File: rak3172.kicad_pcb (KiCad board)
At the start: 4 copper layers, 40 x 30 mm, 82 parts, among them Q1 AO3401, Q2 SI2302, SW1 SW_Push, SW2 SW_Push, U1 AP6683, U2 RAK3172-SiP, U3 TP733xx, U4 UHE4913, U5 QMC6308, U6 L80RE-M37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

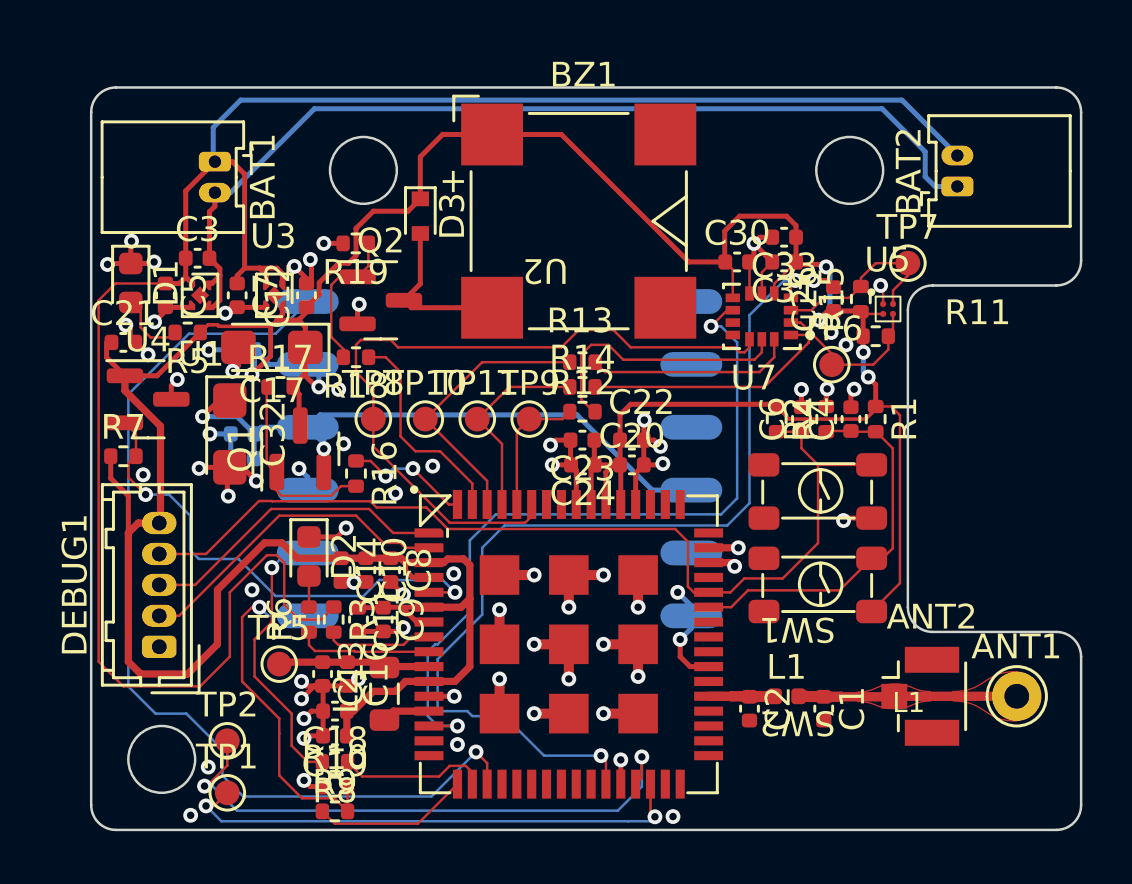
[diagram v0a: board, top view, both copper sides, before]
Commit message: Added 3D Models (-Antenna) Added Manufacturing File (BOM/POS/Gerber) Tidied up silkscreen placement Added via stitching Added via fencing for GCPW Changed bat connector position and package (to SMD)
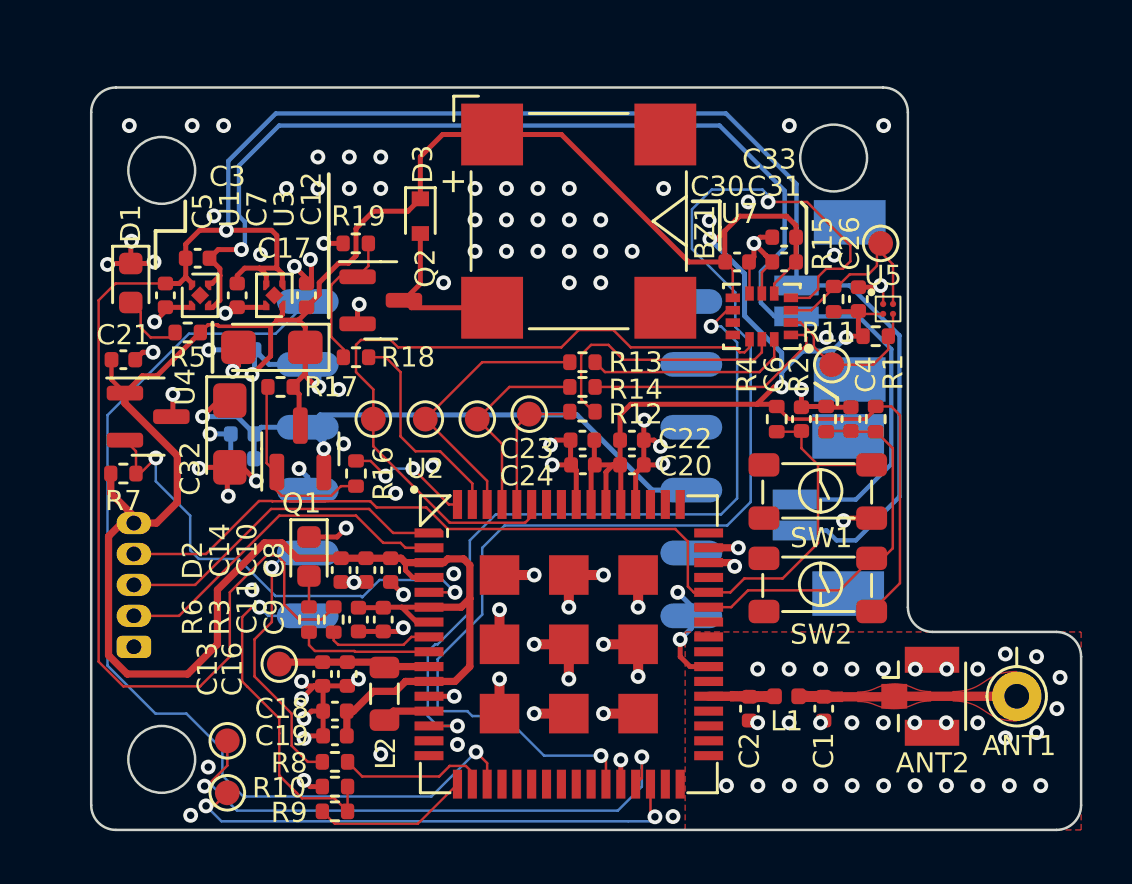
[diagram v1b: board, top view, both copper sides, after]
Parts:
- BAT1, BAT2: footprint Connector_Molex:Molex_PicoBlade_53048-0210_1x02_P1.25mm_Horizontal -> LokapinLib:1.25-2PWB DEALON; moved to B.Cu
- R5: value DNP -> 1k
- moved BAT1 23.6 mm to (208.5, 90.5)
- moved BAT2 12.0 mm to (208.4, 99.1), turned to -90 degrees
- moved TP7 1.36 mm to (211.9, 91.3)
- moved R15 1.10 mm to (210.0, 93.5)
- moved DEBUG1 1.03 mm to (181.7, 107.6)
- moved C26 1.00 mm to (211.0, 93.5)
- moved C21 0.70 mm to (181.3, 96.0)
- moved U4 0.70 mm to (182.3, 98.3)
- moved R7 0.70 mm to (181.3, 100.6)
- moved TP9 0.20 mm to (197.7, 98.2)
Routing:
- net IMU_INT1: track 38.2 -> 52.1 mm
- net -BATT: track 39.1 -> 52.0 mm, vias 0 -> 1
- net +BATT: track 81.5 -> 93.4 mm, vias 0 -> 1
- net +3V3: track 149.4 -> 155.4 mm, vias 6 -> 5
- net NRST: track 38.9 -> 39.9 mm
- net SWDIO: track 12.5 -> 13.6 mm
- net SWCLK: track 13.1 -> 14.1 mm
- net 1PPS: track 39.4 -> 40.1 mm
- net GND: track 80.4 -> 79.9 mm, vias 72 -> 136
- added copper zone on F.Cu, net GND
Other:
- outline, holes or cut-outs redrawn
- board text removed: "L1"
